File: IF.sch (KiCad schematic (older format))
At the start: 42 parts, among them U10 NE5532, U11 MC33079

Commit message: first edit
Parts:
- C44, C47, C59, C60, C61, C63, C64, C66, C67, C68: footprint UI:C_1206_0603 -> Capacitors_SMD:C_0603_HandSoldering
- C45, C58, C62, C65: footprint Capacitors_THT:CP_Radial_D5.0mm_P2.00mm -> Capacitors_Tantalum_SMD:CP_Tantalum_Case-A_EIA-3216-18_Wave
- R37, R38, R39, R40, R41, R42, R43, R44, R45, R46, R47, R48, R49, R50, R51, R52, R53, R54, R55, R56, R57, R58, R59, R60: footprint UI:R_1206_0603 -> Resistors_SMD:R_0603_HandSoldering

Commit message: PCB s1
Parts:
- L7, L8: footprint (none) -> Choke_Axial_ThroughHole:Choke_Horizontal_RM10mm
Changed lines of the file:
@@
 Connection ~ 1700 4150
 $Comp
-L GND #PWR47
+L GND #PWR045
 U 1 1 5EA9849C
 P 1700 4450
-F 0 "#PWR47" H 1700 4200 50  0001 C CNN
+F 0 "#PWR045" H 1700 4200 50  0001 C CNN
 F 1 "GND" H 1700 4300 50  0001 C CNN
 F 2 "" H 1700 4450 50  0001 C CNN
@@
 $EndComp
 $Comp
-L GND #PWR51
+L GND #PWR046
 U 1 1 5EA98567
 P 3000 5400
-F 0 "#PWR51" H 3000 5150 50  0001 C CNN
+F 0 "#PWR046" H 3000 5150 50  0001 C CNN
 F 1 "GND" H 3000 5250 50  0001 C CNN
 F 2 "" H 3000 5400 50  0001 C CNN
@@
 $EndComp
 $Comp
-L GND #PWR50
+L GND #PWR047
 U 1 1 5EA985A2
 P 3000 3450
-F 0 "#PWR50" H 3000 3200 50  0001 C CNN
+F 0 "#PWR047" H 3000 3200 50  0001 C CNN
 F 1 "GND" H 3000 3300 50  0001 C CNN
 F 2 "" H 3000 3450 50  0001 C CNN
@@
 F 0 "L7" H 4280 1590 50  0000 L CNN
 F 1 "22uH" H 4280 1510 50  0000 L CNN
-F 2 "" H 4250 1550 50  0001 C CNN
+F 2 "Choke_Axial_ThroughHole:Choke_Horizontal_RM10mm" H 4250 1550 50  0001 C CNN
 F 3 "" H 4250 1550 50  0001 C CNN
 	1    4250 1550
@@
 	1250 4250 1250 4150
 $Comp
-L GND #PWR46
+L GND #PWR048
 U 1 1 5EA98F43
 P 1250 4450
-F 0 "#PWR46" H 1250 4200 50  0001 C CNN
+F 0 "#PWR048" H 1250 4200 50  0001 C CNN
 F 1 "GND" H 1250 4300 50  0001 C CNN
 F 2 "" H 1250 4450 50  0001 C CNN
@@
 $EndComp
 $Comp
-L GND #PWR45
+L GND #PWR049
 U 1 1 5EA99077
 P 750 4450
-F 0 "#PWR45" H 750 4200 50  0001 C CNN
+F 0 "#PWR049" H 750 4200 50  0001 C CNN
 F 1 "GND" H 750 4300 50  0001 C CNN
 F 2 "" H 750 4450 50  0001 C CNN
@@
 Connection ~ 2550 5200
 $Comp
-L GND #PWR48
+L GND #PWR050
 U 1 1 5EA99826
 P 2150 2050
-F 0 "#PWR48" H 2150 1800 50  0001 C CNN
+F 0 "#PWR050" H 2150 1800 50  0001 C CNN
 F 1 "GND" H 2150 1900 50  0001 C CNN
 F 2 "" H 2150 2050 50  0001 C CNN
@@
 $EndComp
 $Comp
-L GND #PWR49
+L GND #PWR051
 U 1 1 5EA998A3
 P 2650 2050
-F 0 "#PWR49" H 2650 1800 50  0001 C CNN
+F 0 "#PWR051" H 2650 1800 50  0001 C CNN
 F 1 "GND" H 2650 1900 50  0001 C CNN
 F 2 "" H 2650 2050 50  0001 C CNN
@@
 $EndComp
 $Comp
-L GND #PWR61
+L GND #PWR052
 U 1 1 5EA8D0D1
 P 10150 2950
-F 0 "#PWR61" H 10150 2700 50  0001 C CNN
+F 0 "#PWR052" H 10150 2700 50  0001 C CNN
 F 1 "GND" H 10150 2800 50  0001 C CNN
 F 2 "" H 10150 2950 50  0001 C CNN
@@
 $EndComp
 $Comp
-L GND #PWR62
+L GND #PWR053
 U 1 1 5EA8D1C6
 P 10150 4550
-F 0 "#PWR62" H 10150 4300 50  0001 C CNN
+F 0 "#PWR053" H 10150 4300 50  0001 C CNN
 F 1 "GND" H 10150 4400 50  0001 C CNN
 F 2 "" H 10150 4550 50  0001 C CNN
@@
 $EndComp
 $Comp
-L GND #PWR54
+L GND #PWR054
 U 1 1 5EA8D9D2
 P 6300 2800
-F 0 "#PWR54" H 6300 2550 50  0001 C CNN
+F 0 "#PWR054" H 6300 2550 50  0001 C CNN
 F 1 "GND" H 6300 2650 50  0001 C CNN
 F 2 "" H 6300 2800 50  0001 C CNN
@@
 $EndComp
 $Comp
-L GND #PWR56
+L GND #PWR055
 U 1 1 5EA8DB9E
 P 8500 2800
-F 0 "#PWR56" H 8500 2550 50  0001 C CNN
+F 0 "#PWR055" H 8500 2550 50  0001 C CNN
 F 1 "GND" H 8500 2650 50  0001 C CNN
 F 2 "" H 8500 2800 50  0001 C CNN
@@
 $EndComp
 $Comp
-L GND #PWR55
+L GND #PWR056
 U 1 1 5EA8DC1E
 P 6300 4450
-F 0 "#PWR55" H 6300 4200 50  0001 C CNN
+F 0 "#PWR056" H 6300 4200 50  0001 C CNN
 F 1 "GND" H 6300 4300 50  0001 C CNN
 F 2 "" H 6300 4450 50  0001 C CNN
@@
 $EndComp
 $Comp
-L GND #PWR57
+L GND #PWR057
 U 1 1 5EA8DCC5
 P 8500 4450
-F 0 "#PWR57" H 8500 4200 50  0001 C CNN
+F 0 "#PWR057" H 8500 4200 50  0001 C CNN
 F 1 "GND" H 8500 4300 50  0001 C CNN
 F 2 "" H 8500 4450 50  0001 C CNN
@@
 F 0 "L8" H 7230 1690 50  0000 L CNN
 F 1 "22uH" H 7230 1610 50  0000 L CNN
-F 2 "" H 7200 1650 50  0001 C CNN
+F 2 "Choke_Axial_ThroughHole:Choke_Horizontal_RM10mm" H 7200 1650 50  0001 C CNN
 F 3 "" H 7200 1650 50  0001 C CNN
 	1    7200 1650
@@
 Connection ~ 6900 1800
 $Comp
-L GND #PWR59
+L GND #PWR058
 U 1 1 5EA9044E
 P 9250 2400
-F 0 "#PWR59" H 9250 2150 50  0001 C CNN
+F 0 "#PWR058" H 9250 2150 50  0001 C CNN
 F 1 "GND" H 9250 2250 50  0001 C CNN
 F 2 "" H 9250 2400 50  0001 C CNN
@@
 Connection ~ 5950 1800
 $Comp
-L GND #PWR53
+L GND #PWR059
 U 1 1 5EA90E01
 P 5950 2050
-F 0 "#PWR53" H 5950 1800 50  0001 C CNN
+F 0 "#PWR059" H 5950 1800 50  0001 C CNN
 F 1 "GND" H 5950 1900 50  0001 C CNN
 F 2 "" H 5950 2050 50  0001 C CNN
@@
 $EndComp
 $Comp
-L GND #PWR52
+L GND #PWR060
 U 1 1 5EA90F14
 P 5500 2050
-F 0 "#PWR52" H 5500 1800 50  0001 C CNN
+F 0 "#PWR060" H 5500 1800 50  0001 C CNN
 F 1 "GND" H 5500 1900 50  0001 C CNN
 F 2 "" H 5500 2050 50  0001 C CNN
@@
 Connection ~ 9200 3200
 $Comp
-L GND #PWR60
+L GND #PWR061
 U 1 1 5EA92272
 P 9650 3500
-F 0 "#PWR60" H 9650 3250 50  0001 C CNN
+F 0 "#PWR061" H 9650 3250 50  0001 C CNN
 F 1 "GND" H 9650 3350 50  0001 C CNN
 F 2 "" H 9650 3500 50  0001 C CNN
@@
 $EndComp
 $Comp
-L GND #PWR58
+L GND #PWR062
 U 1 1 5EA92391
 P 9200 3500
-F 0 "#PWR58" H 9200 3250 50  0001 C CNN
+F 0 "#PWR062" H 9200 3250 50  0001 C CNN
 F 1 "GND" H 9200 3350 50  0001 C CNN
 F 2 "" H 9200 3500 50  0001 C CNN

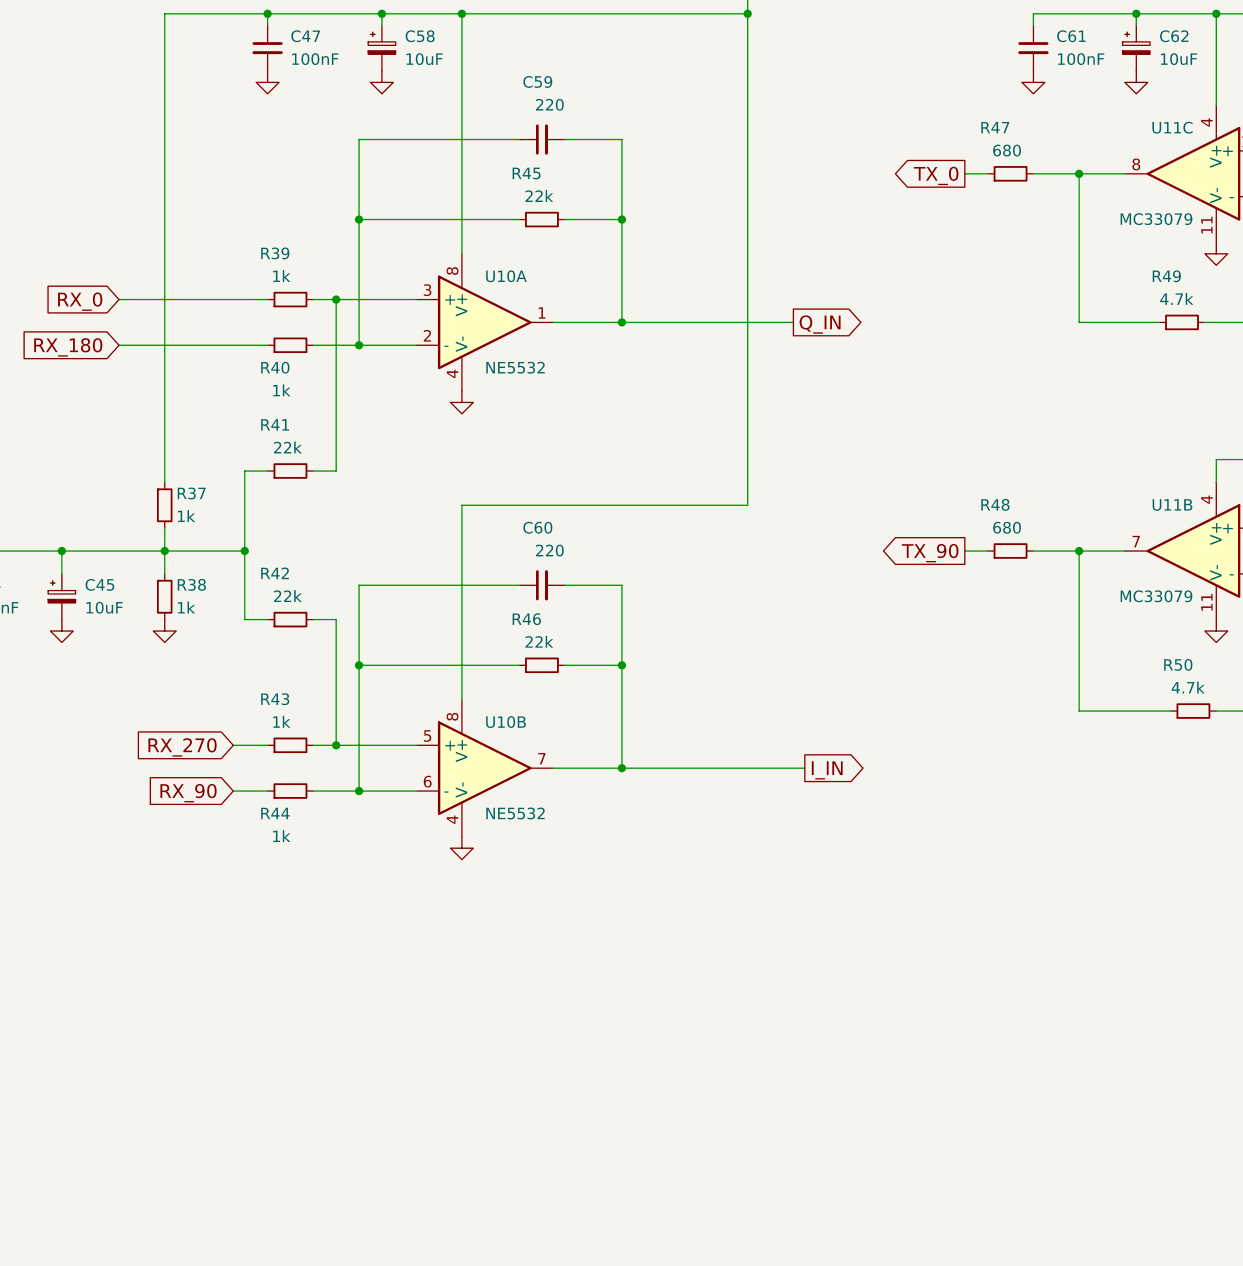
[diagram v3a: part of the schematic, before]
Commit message: need some GND vias
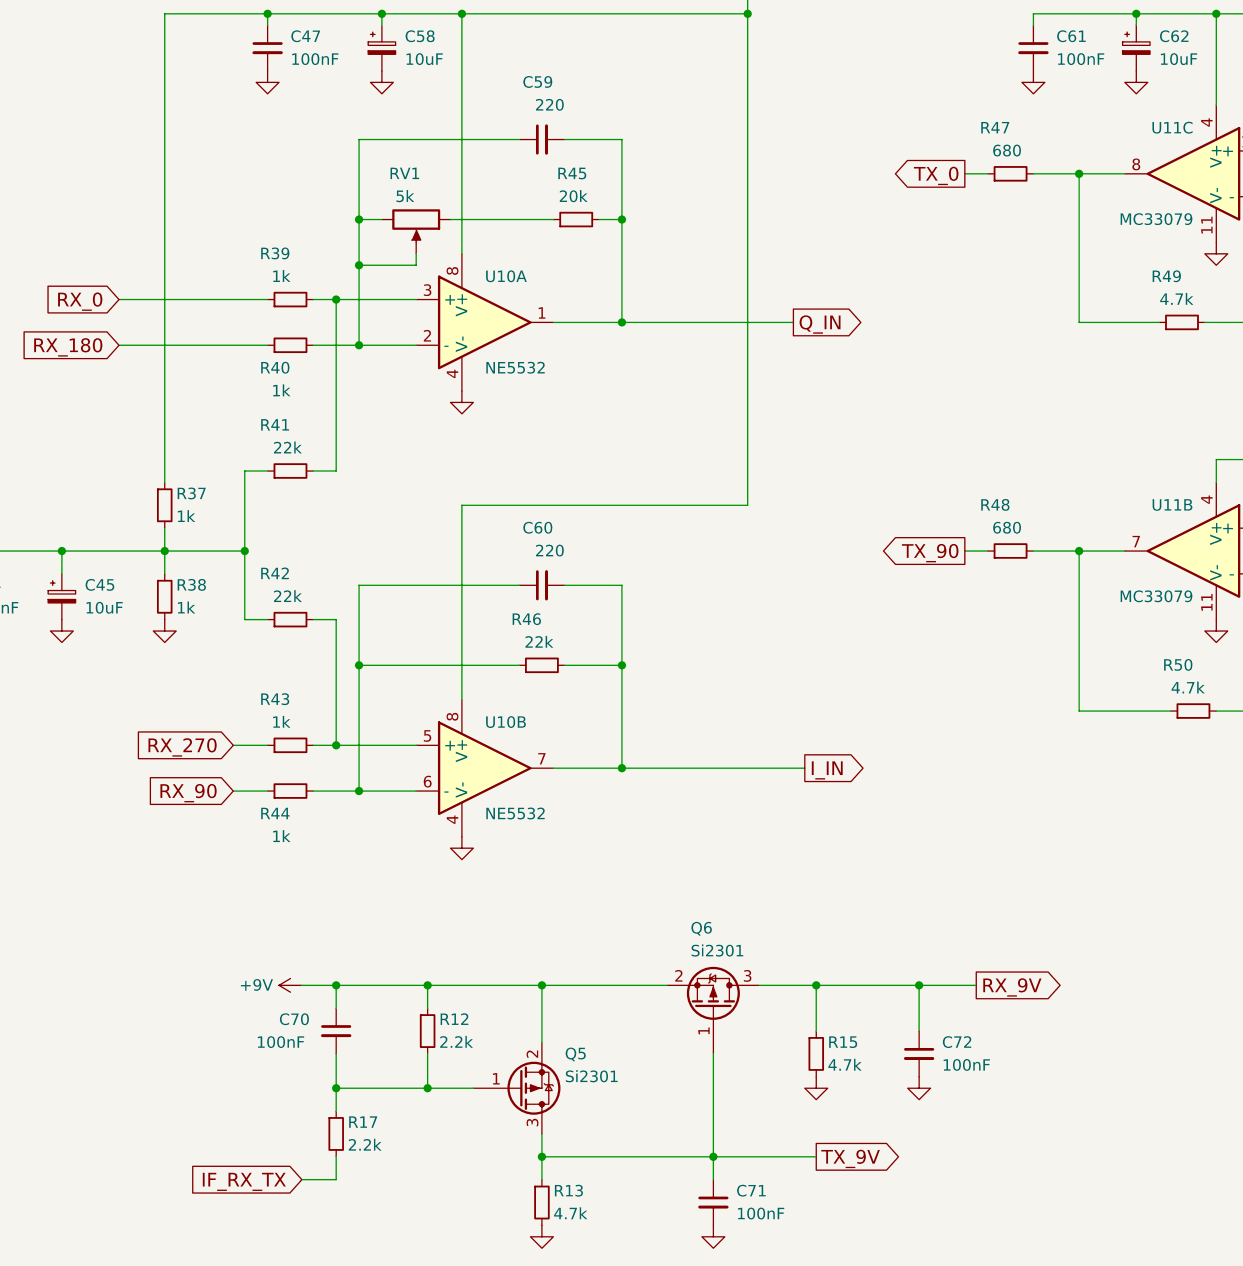
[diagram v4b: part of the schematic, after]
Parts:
- added C70, C71, C72: 100nF, UI:C_1206_0603, symbol C_Small
- added Q5, Q6: Si2301, TO_SOT_Packages_SMD:SOT-23, symbol Q_PMOS_GSD
- added R12, R17: 2.2k, UI:R_1206_0603, symbol R_Small
- added R13, R15: 4.7k, UI:R_1206_0603, symbol R_Small
- added RV1: 5k, UI:Potentiometer_Bourns_3296W_3-8Zoll_Inline_ScrewUp, symbol POT
- C47, C59, C60: footprint Capacitors_SMD:C_0603_HandSoldering -> UI:C_1206_0603
- C58, C62, C65: footprint Capacitors_Tantalum_SMD:CP_Tantalum_Case-A_EIA-3216-18_Wave -> Capacitors_THT:CP_Radial_D5.0mm_P2.00mm
- L8: footprint Choke_Axial_ThroughHole:Choke_Horizontal_RM10mm -> Choke_Axial_ThroughHole:Choke_Horizontal_RM15mm
- R45: value 22k -> 20k; footprint Resistors_SMD:R_0603_HandSoldering -> UI:R_1206_0603
- R46: footprint Resistors_SMD:R_0603_HandSoldering -> UI:R_1206_0603
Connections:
- net GND: now also C71.2, C72.2, R13.2, R15.2
- net RX_9V: now also C72.1, Q6.3 (D), R15.1
- net TX_9V: now also C71.1, Q5.3 (D), Q6.1 (G), R13.1
- net at C59.1, R40.2, U10.2 (-): now also RV1.2, RV1.3; no longer R45.1
- new net: R45.1, RV1.1
- new net: C70.2, Q5.1 (G), R12.2, R17.1
- new net +9V: C70.1, Q5.2 (S), Q6.2 (S), R12.1
- new net IF_RX_TX: R17.2
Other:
- moved on the sheet: R45

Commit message: instrumental amplifier in IF
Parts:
- removed C59, C60: 220, UI:C_1206_0603, symbol C_Small
- removed R39, R40, R43, R44: 1k, Resistors_SMD:R_0603_HandSoldering, symbol R_Small
- removed R41, R42: 22k, Resistors_SMD:R_0603_HandSoldering, symbol R_Small
- removed R45: 20k, UI:R_1206_0603, symbol R_Small
- removed R46: 22k, UI:R_1206_0603, symbol R_Small
- removed RV1: 5k, UI:Potentiometer_Bourns_3296W_3-8Zoll_Inline_ScrewUp, symbol POT
- removed U10: NE5532, Housings_SOIC:SOIC-8_3.9x4.9mm_Pitch1.27mm, symbol NE5532
- added R? (x4): 1k, Resistors_SMD:R_0603_HandSoldering, symbol R_Small
- added R? (x8): 3k, Resistors_SMD:R_0603_HandSoldering, symbol R_Small
- added R? (x2): 270, Resistors_SMD:R_0603_HandSoldering, symbol R_Small
- added U9: MC33079, Housings_SOIC:SOIC-14_3.9x8.7mm_Pitch1.27mm, symbol MC33079
- R37, R38: value 1k -> 750
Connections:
- net GND: now also U9.11 (V-), U9.11 (V-), U9.11 (V-), U9.11 (V-)
- net I_IN: now also R?.2, U9.8
- net Q_IN: now also R?.2, U9.7
- net RX_0: now also R?.2, U9.3 (+)
- net RX_180: now also R?.2, U9.5 (+)
- net RX_270: now also R?.2, U9.12 (+)
- net RX_90: now also R?.2, U9.10 (+)
- net at C47.1, C58.1, L7.2: now also R37.2, U9.4 (V+), U9.4 (V+), U9.4 (V+), U9.4 (V+); no longer R37.1
- net at C44.1, C45.1, R38.1: now also R37.1, R?.1, R?.1, R?.1, R?.1, R?.1, R?.1; no longer R37.2
- new net: R?.1, R?.1, R?.2, U9.9 (-)
- new net: R?.1, R?.1, R?.2, U9.13 (-)
- new net: R?.2, R?.2, U9.14
- new net: R?.2, R?.2, U9.1
- new net: R?.1, R?.1, R?.2, U9.2 (-)
- new net: R?.1, R?.1, R?.2, U9.6 (-)
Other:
- moved on the sheet: C44, C45, C47, C58, C61, C62, C63, C64, C65, C66, C67, C68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

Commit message: PCB 74LCX574
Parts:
- added C1: 100nF, UI:C_1206_0603, symbol C_Small
- C44, C61, C66: footprint Capacitors_SMD:C_0603_HandSoldering -> UI:C_1206_0603
- C45: footprint Capacitors_Tantalum_SMD:CP_Tantalum_Case-A_EIA-3216-18_Wave -> Capacitors_THT:CP_Radial_D5.0mm_P2.00mm
- R37, R38, R57, R58: footprint Resistors_SMD:R_0603_HandSoldering -> UI:R_1206_0603
- gave numbers to parts that had none: 14
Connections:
- net GND: now also C1.2
- net at C44.1, C45.1, R1.1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: now also C1.1
